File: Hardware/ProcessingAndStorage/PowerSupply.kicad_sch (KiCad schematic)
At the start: 6 parts, among them U1 LD1117S50TR_SOT223

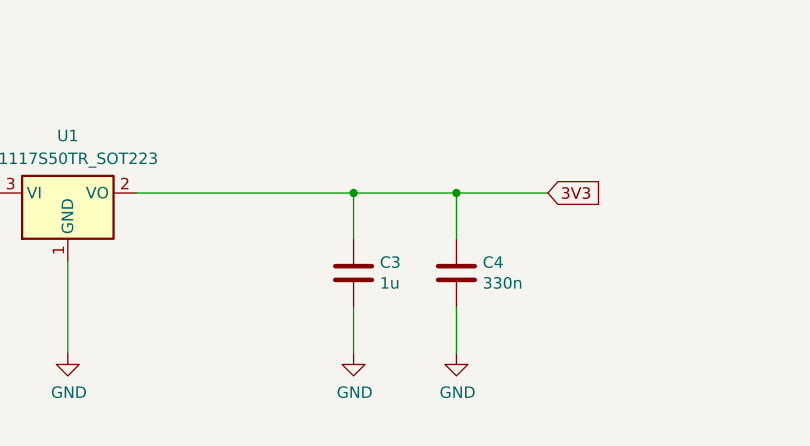
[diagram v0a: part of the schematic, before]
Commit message: make boards smaller, fix sd card slot
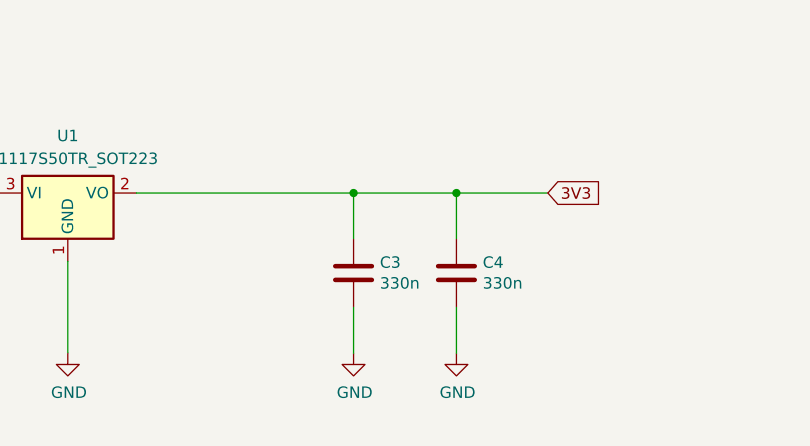
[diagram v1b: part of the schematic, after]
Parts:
- C3: value 1u -> 330n
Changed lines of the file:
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@@
 			)
 		)
-		(property "Value" "1u"
+		(property "Value" "330n"
 			(at 156.591 105.283 0)
 			(effects
